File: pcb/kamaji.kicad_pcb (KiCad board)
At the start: 2 copper layers, 130 x 110 mm, 31 parts, among them J1 RJ10, J2 RJ10, J3 RJ10, J4 RJ10, J5 RJ10, Q1 TIP120, Q2 TIP120, SW1 CTRL1, SW2 CTRL2, SW3 CTRL3, U1 ATMEGA328P-PU

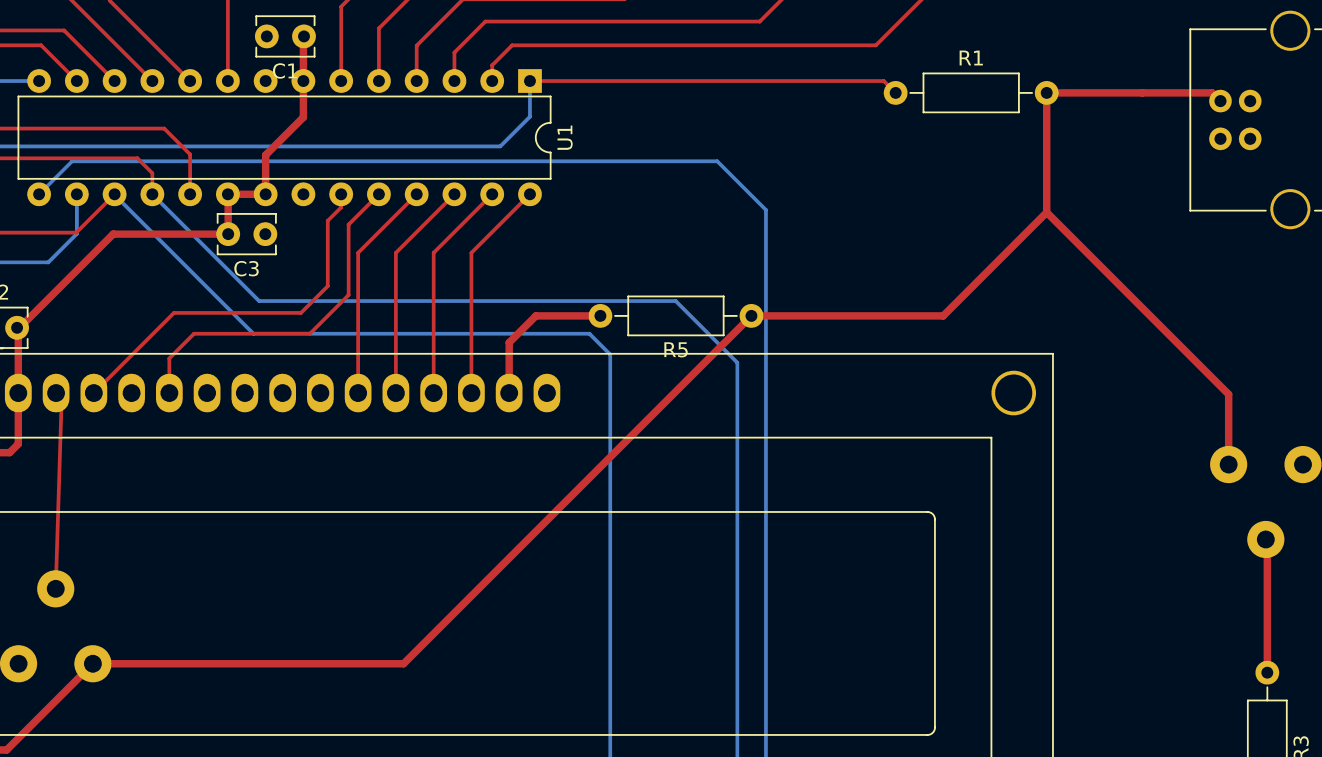
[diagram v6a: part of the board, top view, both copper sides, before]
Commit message: re-route a resistor
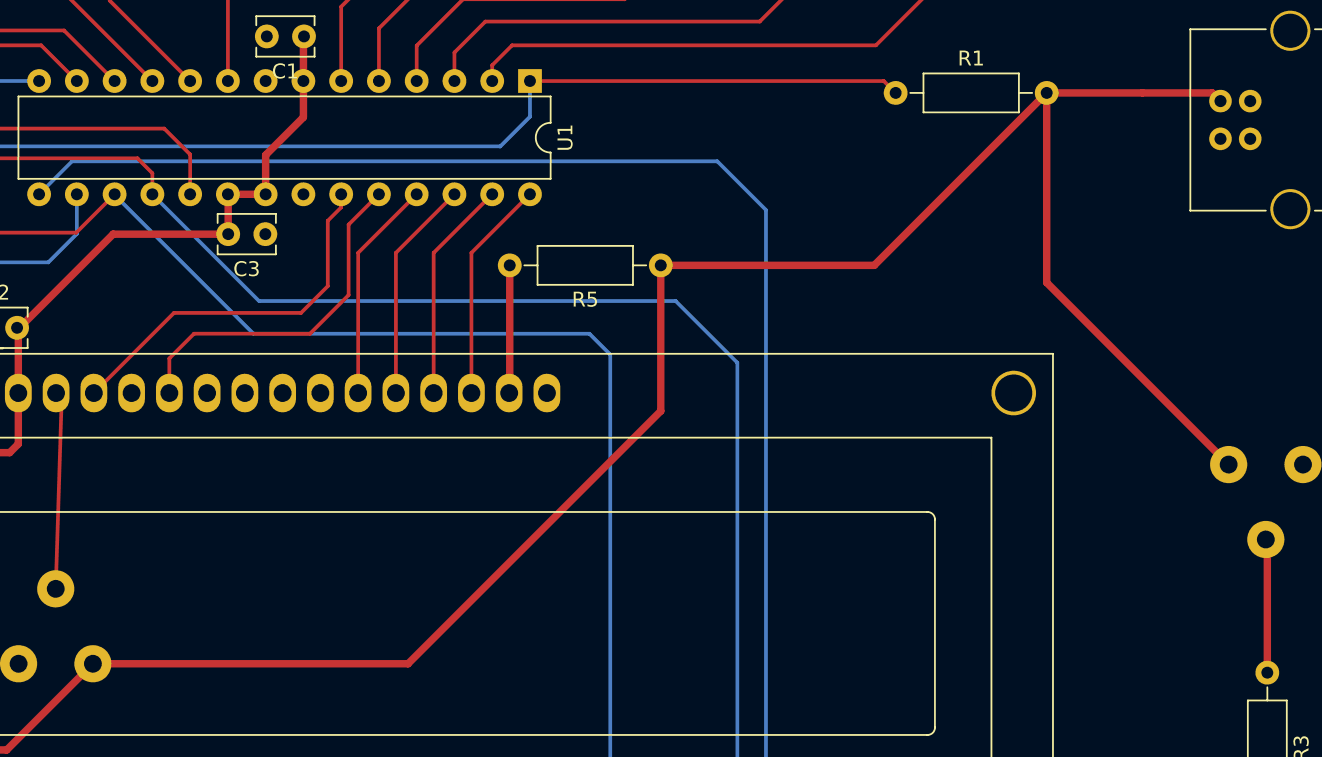
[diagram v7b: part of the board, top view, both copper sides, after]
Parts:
- moved R5 6.98 mm to (178.6, 63.8)
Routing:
- net VCC: track 230.8 -> 239.9 mm
- net Net-(DS1-Pad15): track 11.1 -> 9.50 mm
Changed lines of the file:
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@@
     (links 87)
     (no_connects 3)
-    (area 99.924999 29.924999 230.075001 140.075001)
+    (area 98.074999 29.55 231.725001 140.075001)
     (thickness 1.6)
     (drawings 5)
@@
   (layers
     (0 F.Cu signal)
-    (31 B.Cu signal hide)
+    (31 B.Cu signal)
     (32 B.Adhes user)
     (33 F.Adhes user)
@@
     (pad_to_mask_clearance 0.2)
     (aux_axis_origin 106.4 35.8)
-    (visible_elements FFFFFF7F)
+    (visible_elements FFFFEF7F)
     (pcbplotparams
       (layerselection 0x00030_80000001)
@@
   )
   (module Resistors_THT:R_Axial_DIN0207_L6.3mm_D2.5mm_P10.16mm_Horizontal (layer F.Cu)
-    (at 184.7 67.2 180)
+    (at 178.6 63.8 180)
     (descr "Resistor, Axial_DIN0207 series, Axial, Horizontal, pin pitch=10.16mm, 0.25W = 1/4W, length*diameter=6.3*2.5mm^2, http://cdn-reichelt.de/documents/datenblatt/B400/1_4W%23YAG.pdf")
     (tags "Resistor Axial_DIN0207 series Axial Horizontal pin pitch 10.16mm 0.25W = 1/4W length 6.3mm diameter 2.5mm")
@@
   (target plus (at 165 95.08) (size 5) (width 0.15) (layer Edge.Cuts))
   (gr_line (start 230 140) (end 100 140) (angle 90) (layer Edge.Cuts) (width 0.15))
-  (segment (start 216.8 77.2) (end 216.8 72.48) (width 0.5) (layer F.Cu) (net 1) (status 400000))
-  (segment (start 216.8 72.48) (end 204.56 60.24) (width 0.5) (layer F.Cu) (net 1))
-  (segment (start 184.7 67.2) (end 197.6 67.2) (width 0.5) (layer F.Cu) (net 1) (status 400000))
-  (segment (start 204.56 60.24) (end 204.56 52.2) (width 0.5) (layer F.Cu) (net 1) (status 800000))
-  (segment (start 197.6 67.2) (end 204.56 60.24) (width 0.5) (layer F.Cu) (net 1))
-  (segment (start 140.4 90.6) (end 161.3 90.6) (width 0.5) (layer F.Cu) (net 1) (status 400000))
-  (segment (start 161.3 90.6) (end 184.7 67.2) (width 0.5) (layer F.Cu) (net 1) (status 800000))
+  (segment (start 178.6 63.8) (end 192.96 63.8) (width 0.5) (layer F.Cu) (net 1))
+  (segment (start 192.96 63.8) (end 204.56 52.2) (width 0.5) (layer F.Cu) (net 1))
+  (segment (start 140.4 90.6) (end 161.6 90.6) (width 0.5) (layer F.Cu) (net 1))
+  (segment (start 178.6 73.6) (end 178.6 63.8) (width 0.5) (layer F.Cu) (net 1))
+  (segment (start 161.6 90.6) (end 178.6 73.6) (width 0.5) (layer F.Cu) (net 1))
+  (segment (start 204.56 52.2) (end 204.56 64.96) (width 0.5) (layer F.Cu) (net 1))
+  (segment (start 204.56 64.96) (end 216.8 77.2) (width 0.5) (layer F.Cu) (net 1))
   (segment (start 135.382 72.39) (end 135.382 68.082) (width 0.5) (layer F.Cu) (net 1))
   (segment (start 135.382 68.082) (end 141.764 61.7) (width 0.5) (layer F.Cu) (net 1))
@@
   (segment (start 165.862 72.39) (end 165.862 62.958) (width 0.25) (layer F.Cu) (net 13))
   (segment (start 165.862 62.958) (end 169.8 59.02) (width 0.25) (layer F.Cu) (net 13))
-  (segment (start 168.402 72.39) (end 168.402 68.998) (width 0.5) (layer F.Cu) (net 14) (status 400000))
-  (segment (start 170.2 67.2) (end 174.54 67.2) (width 0.5) (layer F.Cu) (net 14) (status 800000))
-  (segment (start 168.402 68.998) (end 170.2 67.2) (width 0.5) (layer F.Cu) (net 14))
+  (segment (start 168.44 63.8) (end 168.44 72.352) (width 0.5) (layer F.Cu) (net 14))
+  (segment (start 168.44 72.352) (end 168.402 72.39) (width 0.5) (layer F.Cu) (net 14))
+  (segment (start 168.44 72.352) (end 168.402 72.39) (width 0.5) (layer F.Cu) (net 14))
   (segment (start 168.6 72.588) (end 168.402 72.39) (width 0.5) (layer F.Cu) (net 14))
   (segment (start 168.8 72.788) (end 168.402 72.39) (width 0.25) (layer F.Cu) (net 14))

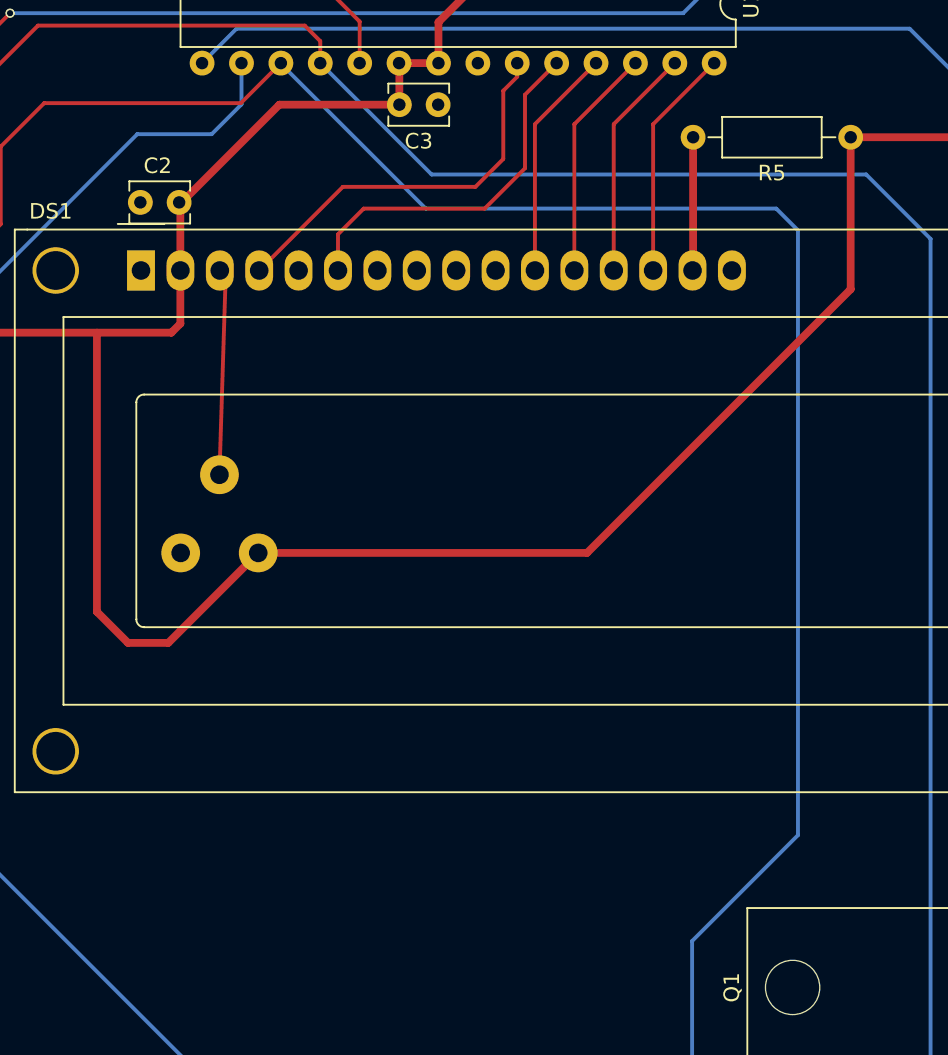
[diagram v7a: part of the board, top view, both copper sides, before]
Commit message: re-route a potentiometer
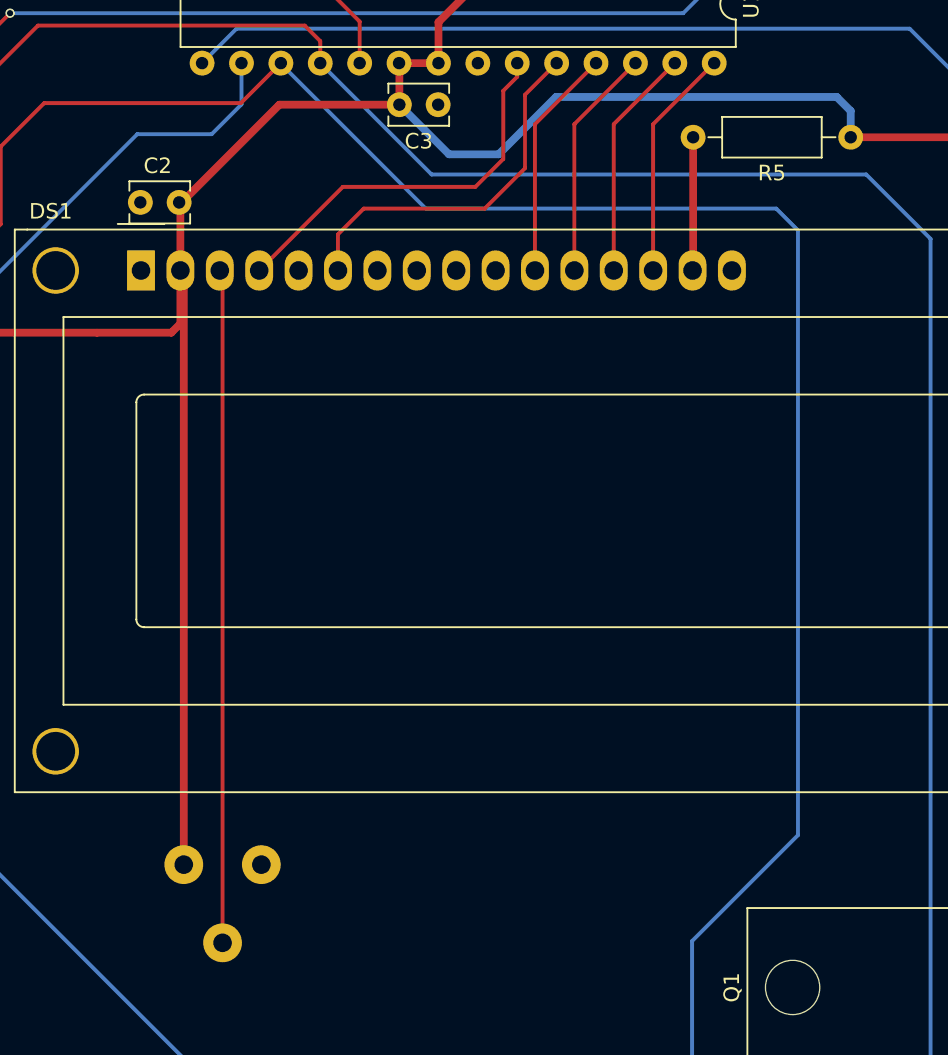
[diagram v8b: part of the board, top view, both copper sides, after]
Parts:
- moved RV2 20.7 mm to (135.6, 110.7), turned to 0 degrees
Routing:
- net Net-(DS1-Pad3): track 13.3 -> 44.3 mm
- net VCC: track 239.9 -> 225.6 mm
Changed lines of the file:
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@@
     (thickness 1.6)
     (drawings 5)
-    (tracks 185)
+    (tracks 189)
     (zones 0)
     (modules 31)
@@
   )
   (module Potentiometers:Potentiometer_Triwood_RM-065 (layer B.Cu)
-    (at 140.4 90.6 180)
+    (at 135.6 110.7)
     (descr "Potentiometer, Trimmer, RM-065")
     (tags "Potentiometer Trimmer RM-065")
-    (fp_text reference RV2 (at -2.1 2.5 450) (layer B.SilkS)
+    (fp_text reference RV2 (at -2.1 2.5 270) (layer B.SilkS)
       (effects (font (size 1 1) (thickness 0.15)) (justify mirror))
     )
-    (fp_text value POT (at 7.5 2.5 450) (layer B.Fab)
+    (fp_text value POT (at 7.5 2.5 270) (layer B.Fab)
       (effects (font (size 1 1) (thickness 0.15)) (justify mirror))
     )
@@
     (fp_arc (start 2.5 2.5) (end 3.39 3.9) (angle -90) (layer B.Fab) (width 0.1))
     (fp_arc (start 2.5 2.5) (end 1.1 1.61) (angle -90) (layer B.Fab) (width 0.1))
-    (pad 2 thru_hole circle (at 2.5 5.04 180) (size 2.5 2.5) (drill 1.2) (layers *.Cu *.Mask)
+    (pad 2 thru_hole circle (at 2.5 5.04) (size 2.5 2.5) (drill 1.2) (layers *.Cu *.Mask)
       (net 3 "Net-(DS1-Pad3)"))
-    (pad 3 thru_hole circle (at 5 0 180) (size 2.5 2.5) (drill 1.2) (layers *.Cu *.Mask)
-      (net 2 GND))
-    (pad 1 thru_hole circle (at 0 0 180) (size 2.5 2.5) (drill 1.2) (layers *.Cu *.Mask)
+    (pad 3 thru_hole circle (at 5 0) (size 2.5 2.5) (drill 1.2) (layers *.Cu *.Mask)
+      (net 2 GND))
+    (pad 1 thru_hole circle (at 0 0) (size 2.5 2.5) (drill 1.2) (layers *.Cu *.Mask)
       (net 1 VCC))
     (model Potentiometers.3dshapes/Potentiometer_Triwood_RM-065.wrl
@@
   (target plus (at 165 95.08) (size 5) (width 0.15) (layer Edge.Cuts))
   (gr_line (start 230 140) (end 100 140) (angle 90) (layer Edge.Cuts) (width 0.15))
+  (segment (start 178.6 63.8) (end 178.6 62.1) (width 0.5) (layer B.Cu) (net 1))
+  (segment (start 152.7 64.9) (end 149.5 61.7) (width 0.5) (layer B.Cu) (net 1))
+  (segment (start 155.9 64.9) (end 152.7 64.9) (width 0.5) (layer B.Cu) (net 1))
+  (segment (start 159.6 61.2) (end 155.9 64.9) (width 0.5) (layer B.Cu) (net 1))
+  (segment (start 177.7 61.2) (end 159.6 61.2) (width 0.5) (layer B.Cu) (net 1))
+  (segment (start 178.6 62.1) (end 177.7 61.2) (width 0.5) (layer B.Cu) (net 1))
+  (segment (start 135.6 110.7) (end 135.6 72.608) (width 0.5) (layer F.Cu) (net 1))
+  (segment (start 135.6 72.608) (end 135.382 72.39) (width 0.5) (layer F.Cu) (net 1))
   (segment (start 178.6 63.8) (end 192.96 63.8) (width 0.5) (layer F.Cu) (net 1))
   (segment (start 192.96 63.8) (end 204.56 52.2) (width 0.5) (layer F.Cu) (net 1))
-  (segment (start 140.4 90.6) (end 161.6 90.6) (width 0.5) (layer F.Cu) (net 1))
-  (segment (start 178.6 73.6) (end 178.6 63.8) (width 0.5) (layer F.Cu) (net 1))
-  (segment (start 161.6 90.6) (end 178.6 73.6) (width 0.5) (layer F.Cu) (net 1))
   (segment (start 204.56 52.2) (end 204.56 64.96) (width 0.5) (layer F.Cu) (net 1))
   (segment (start 204.56 64.96) (end 216.8 77.2) (width 0.5) (layer F.Cu) (net 1))
@@
   (segment (start 154.56 48.44) (end 154.6 48.4) (width 0.5) (layer F.Cu) (net 1))
   (segment (start 151.9 59.14) (end 152.02 59.02) (width 0.5) (layer F.Cu) (net 1))
-  (segment (start 130 76.4) (end 130 94.4) (width 0.5) (layer F.Cu) (net 1))
-  (segment (start 130 94.4) (end 132 96.4) (width 0.5) (layer F.Cu) (net 1))
-  (segment (start 132 96.4) (end 134.6 96.4) (width 0.5) (layer F.Cu) (net 1))
-  (segment (start 134.6 96.4) (end 140.4 90.6) (width 0.5) (layer F.Cu) (net 1))
   (segment (start 204.56 52.2) (end 211 52.2) (width 0.5) (layer F.Cu) (net 1))
   (segment (start 211 52.2) (end 215.7 52.2) (width 0.5) (layer F.Cu) (net 1))
@@
   (segment (start 108.83 73.79) (end 115.08 67.54) (width 0.5) (layer B.Cu) (net 2))
   (segment (start 154.4 59.18) (end 154.56 59.02) (width 0.5) (layer F.Cu) (net 2))
-  (segment (start 137.9 85.56) (end 138.3 72.768) (width 0.25) (layer F.Cu) (net 3) (status 10))
+  (segment (start 138.1 115.74) (end 138.1 72.568) (width 0.25) (layer F.Cu) (net 3))
+  (segment (start 138.1 72.568) (end 137.922 72.39) (width 0.25) (layer F.Cu) (net 3))
+  (segment (start 138.1 72.568) (end 137.922 72.39) (width 0.25) (layer B.Cu) (net 3))
+  (segment (start 138 72.468) (end 137.922 72.39) (width 0.25) (layer F.Cu) (net 3))
   (segment (start 138.3 72.768) (end 137.922 72.39) (width 0.25) (layer F.Cu) (net 3))
   (segment (start 157.1 59.02) (end 157.1 59.9) (width 0.25) (layer F.Cu) (net 4))
